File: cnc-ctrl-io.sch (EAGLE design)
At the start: 76 parts, among them IC1 MAX304SE, IC2 MAX304SE, IC8 MAX3072EESA, J2 22-05-7048-04, U1 TLC082D

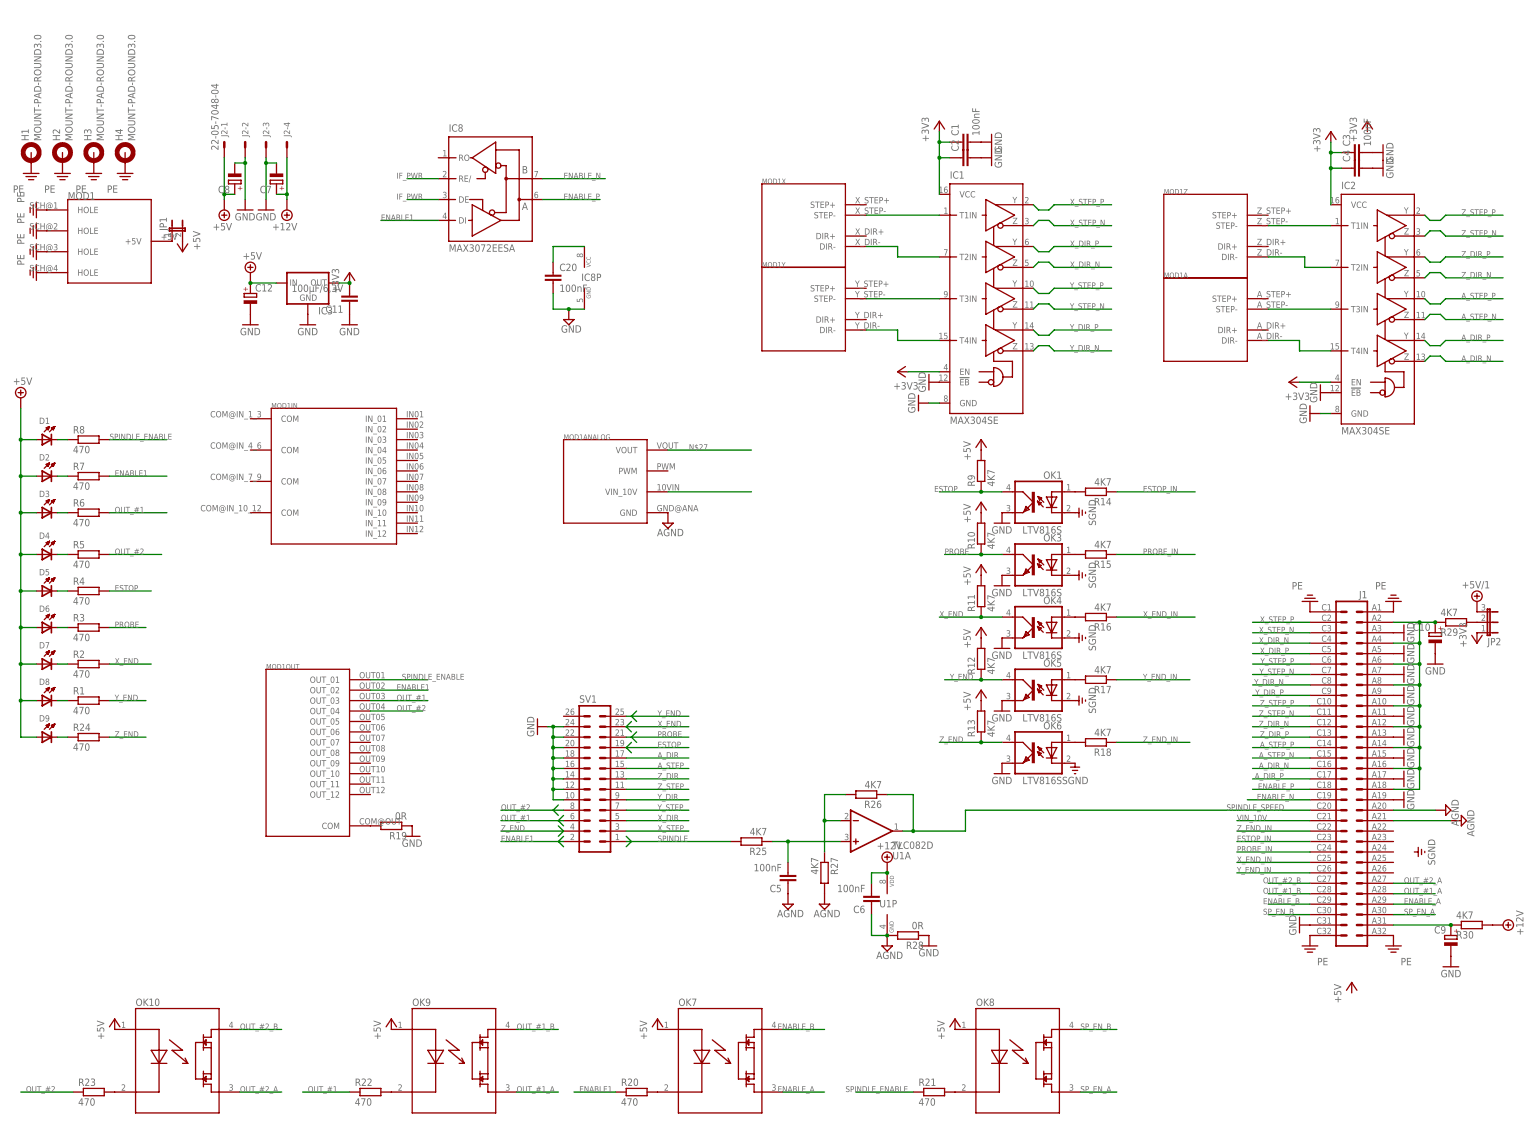
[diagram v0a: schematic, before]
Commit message: DDLMV1-Inputs hinzugefügt @work
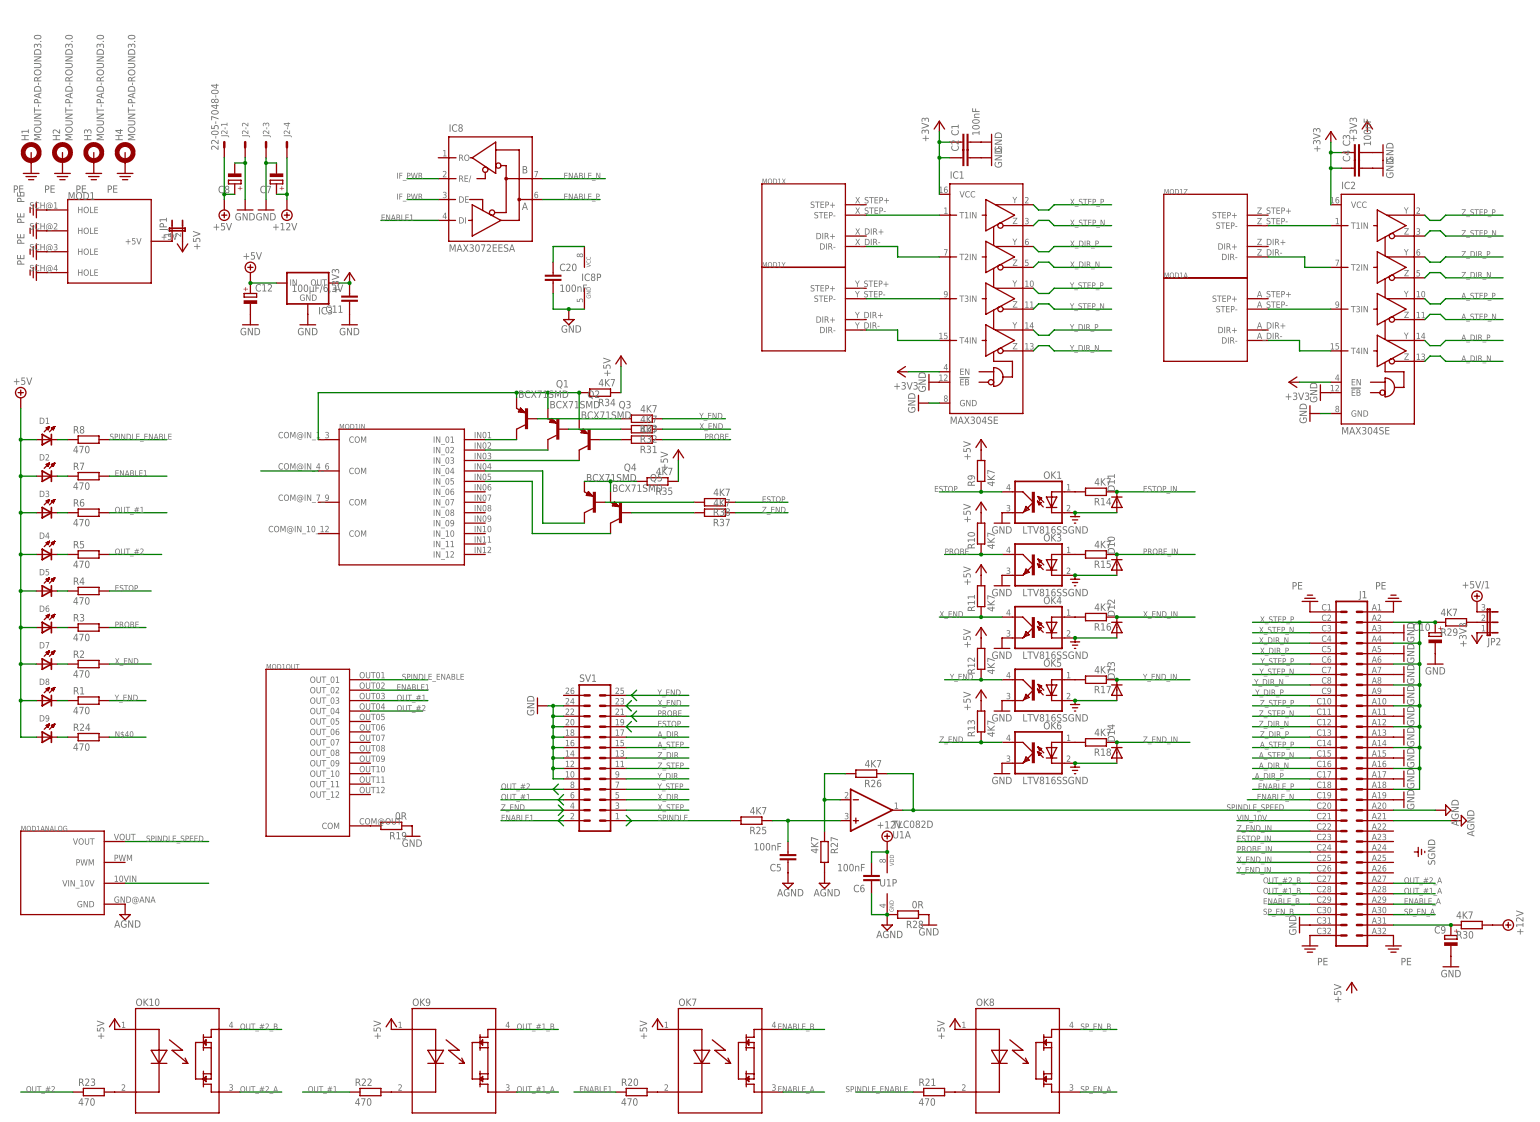
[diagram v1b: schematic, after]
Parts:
- added D10, D11, D12, D13, D14: (no value), diode:DIODE-SMB
- added Q1, Q2, Q3, Q4, Q5: BCX71SMD, transistor-pnp:BCX71SMD
- added R31, R32, R33, R34, R35, R37, R38: 4K7, rcl:R-EU_R0603
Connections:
- new net COM@IN_1_3: MOD1IN.COM@IN_1_3, Q1.E, Q2.E, Q3.E, R34.2
- new net COM@IN_4_6: MOD1IN.COM@IN_4_6, Q4.E, Q5.E, R35.2
- new net N$21: MOD1IN.IN_01, Q1.C
- new net N$28: MOD1IN.IN_03, Q3.C
- new net N$29: MOD1IN.IN_04, Q4.C
- new net N$30: Q3.B, R31.2
- new net N$31: Q2.B, R32.2
- new net N$32: Q1.B, R33.2
- new net N$33: MOD1IN.IN_05, Q5.C
- new net N$36: Q5.B, R37.2
- new net N$37: Q4.B, R38.2
- new net N$40: R24.2
- net +5V: now also R34.1, R35.1
- net ESTOP: now also R38.1
- net ESTOP_IN: now also D11.C
- net N$27: now also MOD1IN.IN_02, Q2.C; no longer MOD1ANALOG.VOUT
- net PROBE: now also R31.1
- net PROBE_IN: now also D10.C
- net SGND: now also D10.A, D11.A, D12.A, D13.A, D14.A
- net SPINDLE_SPEED: now also MOD1ANALOG.VOUT
- net X_END: now also R32.1
- net X_END_IN: now also D12.C
- net Y_END: now also R33.1
- net Y_END_IN: now also D13.C
- net Z_END: now also R37.1; no longer R24.2
- net Z_END_IN: now also D14.C
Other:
- moved on the sheet: C5, C6, MOD1ANALOG, MOD1IN, R25, R26, R27, R28, SV1, U1A, U1P

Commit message: Routing fertig @work
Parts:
- added R36: 4K7, rcl:R-EU_R0603
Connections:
- removed net +5V/1: JP2.3
- removed net N$19: OK10.2, R23.2
- removed net N$40: R24.2
- new net 12V: C6.2, C9.+, J1.A31, R30.1, U1P.VDD
- net +12V: no longer C6.2, U1P.VDD
- net +3V3: now also C20.1, IC8G$1.DE, IC8G$1.RE/, IC8P.VCC, R36.1
- net +5V: now also JP2.3
- net ENABLE1: now also R36.2
- net IF_PWR: no longer C20.1, IC8P.VCC
- net N$1: now also OK9.2, R23.2; no longer C9.+, J1.A31, R30.1
- net N$18: now also OK10.2; no longer OK9.2
- net OUT_#1_A: now also J1.A27, OK10.3; no longer J1.A28, OK9.3
- net OUT_#1_B: now also J1.C27, OK10.4; no longer J1.C28, OK9.4
- net OUT_#2_A: now also J1.A28, OK9.3; no longer J1.A27, OK10.3
- net OUT_#2_B: now also J1.C28, OK9.4; no longer J1.C27, OK10.4
- net SGND: now also J1.A22, J1.A23, J1.A24, J1.A25, J1.A26
- net Z_END: now also R24.2
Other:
- moved on the sheet: C20, IC8, IC8P, R22, R23

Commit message: lpt-connector verschoben, beschaltung für schirmung angepasst
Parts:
- added R39: 1M, rcl:R-EU_R0603
- added U$1: 0,01µF, Capacitor-Wima-MKS4-250v:0,01µF
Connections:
- net GND: now also R39.2, U$1.2
- net PE: now also R39.1, U$1.1
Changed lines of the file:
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@@
 <part name="+3V10" library="supply1" deviceset="+3V3" device=""/>
 <part name="+3V11" library="supply1" deviceset="+3V3" device=""/>
+<part name="SUPPLY2" library="supply2" deviceset="PE" device=""/>
+<part name="R39" library="rcl" deviceset="R-EU_" device="R0603" value="1M"/>
+<part name="GND21" library="supply1" deviceset="GND" device=""/>
+<part name="U$1" library="Capacitor-Wima-MKS4-250v" deviceset="0,01µF" device=""/>
 </parts>
 <sheets>
@@
 <instance part="+3V10" gate="G$1" x="142.24" y="219.71" rot="R90"/>
 <instance part="+3V11" gate="G$1" x="142.24" y="214.63" rot="R90"/>
+<instance part="SUPPLY2" gate="PE" x="15.24" y="201.93" rot="R270"/>
+<instance part="R39" gate="G$1" x="22.86" y="201.93"/>
+<instance part="GND21" gate="1" x="30.48" y="201.93" rot="R90"/>
+<instance part="U$1" gate="G$1" x="22.86" y="196.85"/>
 </instances>
 <busses>
@@
 <pinref part="SUPPLY33" gate="GND" pin="GND"/>
 <pinref part="C20" gate="G$1" pin="2"/>
+</segment>
+<segment>
+<pinref part="R39" gate="G$1" pin="2"/>
+<pinref part="GND21" gate="1" pin="GND"/>
+<wire x1="27.94" y1="201.93" x2="27.94" y2="196.85" width="0.1524" layer="91"/>
+<pinref part="U$1" gate="G$1" pin="2"/>
+<wire x1="27.94" y1="196.85" x2="25.4" y2="196.85" width="0.1524" layer="91"/>
+<junction x="27.94" y="201.93"/>
 </segment>
 </net>
@@
 <pinref part="SUPPLY14" gate="PE" pin="PE"/>
 </segment>
-</net>
+<segment>
+<pinref part="SUPPLY2" gate="PE" pin="PE"/>
+<pinref part="R39" gate="G$1" pin="1"/>
+<pinref part="U$1" gate="G$1" pin="1"/>
+<wire x1="20.32" y1="196.85" x2="17.78" y2="196.85" width="0.1524" layer="91"/>
+<wire x1="17.78" y1="196.85" x2="17.78" y2="201.93" width="0.1524" layer="91"/>
+<junction x="17.78" y="201.93"/>
+</segment>
+</net>
